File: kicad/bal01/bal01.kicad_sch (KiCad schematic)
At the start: 8 parts, among them IC1 AS5600/1-ASOT

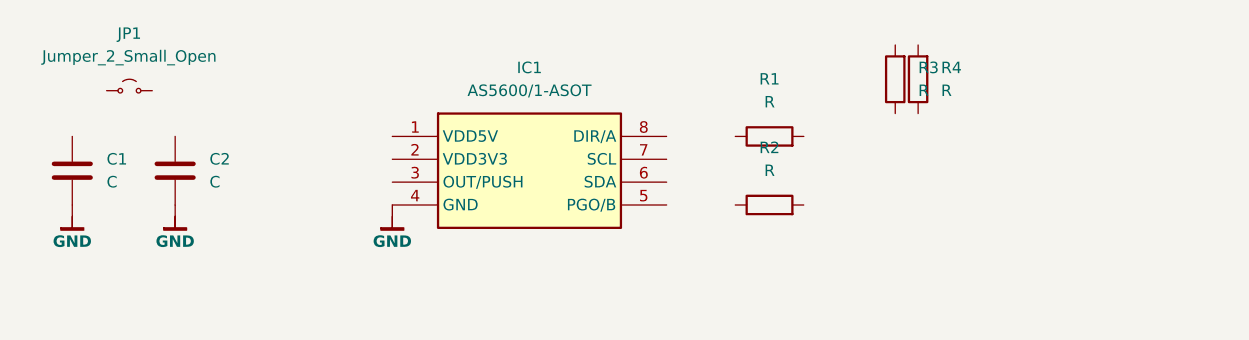
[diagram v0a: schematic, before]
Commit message: create new pcb with AS5601
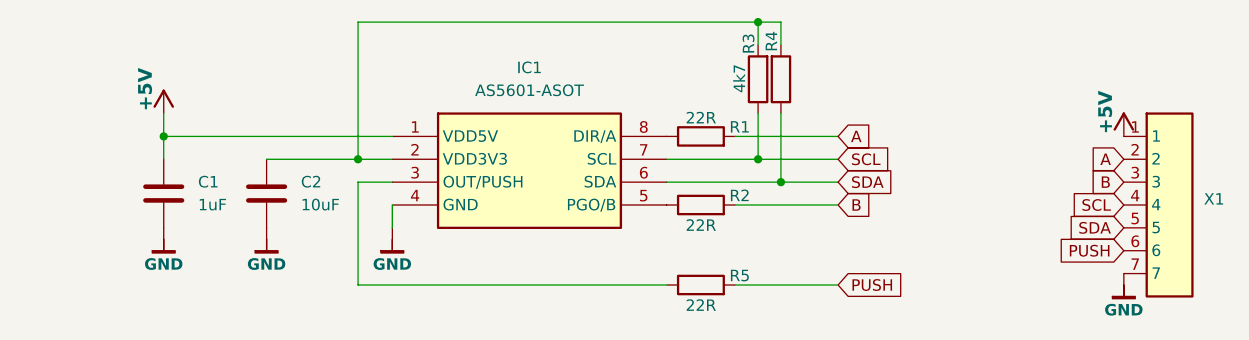
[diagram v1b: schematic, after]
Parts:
- removed JP1: Jumper_2_Small_Open, symbol Jumper:Jumper_2_Small_Open
- added R5: 22R, Capacitor_SMD:C_0603_1608Metric, symbol Device:R
- added X1: ~, bal:H7_Pads_1.27mm, symbol bal_symbols:H7
- C1: value C -> 1uF; footprint (none) -> Capacitor_SMD:C_0805_2012Metric
- C2: value C -> 10uF; footprint (none) -> Capacitor_SMD:C_0805_2012Metric
- IC1: value AS5600/1-ASOT -> AS5601-ASOT
- R1, R2: value R -> 22R; footprint (none) -> Capacitor_SMD:C_0603_1608Metric
- R3, R4: value R -> 4k7; footprint (none) -> Capacitor_SMD:C_0603_1608Metric
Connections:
- net GND: now also X1.7
- net at R1.1: now also IC1.8 (DIR/A)
- net A: now reaches R1.2
- net A: now also X1.2
- net SCL: now reaches R3.1
- net SCL: now also IC1.7 (SCL), X1.4
- net at R3.2: now also C2.1, IC1.2 (VDD3V3), R4.2
- net SDA: now reaches R4.1
- net SDA: now also IC1.6 (SDA), X1.5
- net +5V: now reaches C1.1
- net +5V: now also IC1.1 (VDD5V), X1.1
- net at R2.1: now also IC1.5 (PGO/B)
- net B: now reaches R2.2
- net B: now also X1.3
- net at IC1.3 (OUT/PUSH): now also R5.1
- new net PUSH: R5.2, X1.6
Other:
- moved on the sheet: C1, C2, R1, R2, R3, R4

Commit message: bal01 olmost finished
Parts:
- X1: footprint bal:H7_Pads_1.27mm -> bal:H7_Pads_1.27mm-001
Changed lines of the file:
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@@
 			)
 		)
-		(property "Footprint" "bal:H7_Pads_1.27mm"
+		(property "Footprint" "bal:H7_Pads_1.27mm-001"
 			(at 215.9 100.33 0)
 			(effects
